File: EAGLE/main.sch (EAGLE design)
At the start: 5 parts

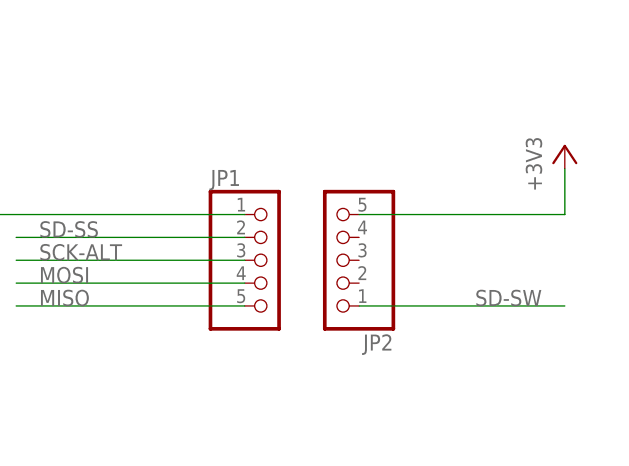
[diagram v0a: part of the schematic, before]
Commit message: Add note about 3V3 solder bridge on SD card PCB
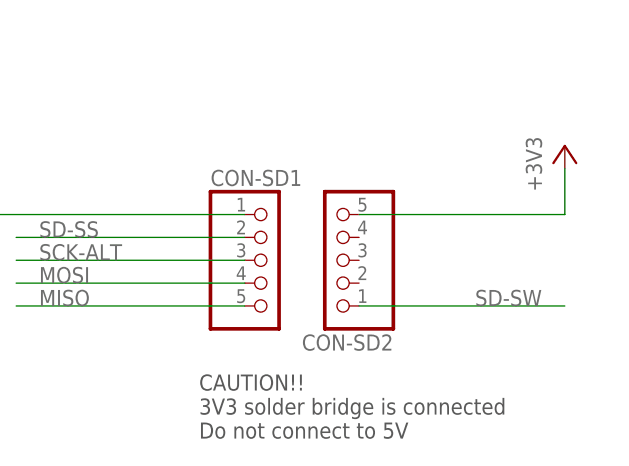
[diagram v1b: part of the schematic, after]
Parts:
- renumbered JP1 to CON-SD1, JP2 to CON-SD2
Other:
- note added: "CAUTION!! 3V3 solder bridge is connected Do not connect to 5V"
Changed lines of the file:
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@@
 <part name="CON-BT" library="pinhead" deviceset="PINHD-1X4" device=""/>
 <part name="CON-GY-80" library="pinhead" deviceset="PINHD-1X4" device=""/>
-<part name="JP1" library="pinhead" deviceset="PINHD-1X5" device=""/>
-<part name="JP2" library="pinhead" deviceset="PINHD-1X5" device=""/>
+<part name="CON-SD1" library="pinhead" deviceset="PINHD-1X5" device=""/>
+<part name="CON-SD2" library="pinhead" deviceset="PINHD-1X5" device=""/>
 <part name="+3V2" library="supply1" deviceset="+3V3" device=""/>
 <part name="GND2" library="supply1" deviceset="GND" device=""/>
@@
 <sheet>
 <plain>
+<text x="149.86" y="55.88" size="1.778" layer="97" rot="MR180">CAUTION!!
+3V3 solder bridge is connected
+Do not connect to 5V</text>
 </plain>
 <instances>
@@
 <instance part="CON-BT" gate="A" x="162.56" y="152.4"/>
 <instance part="CON-GY-80" gate="A" x="162.56" y="111.76"/>
-<instance part="JP1" gate="A" x="157.48" y="68.58"/>
-<instance part="JP2" gate="A" x="165.1" y="68.58" rot="R180"/>
+<instance part="CON-SD1" gate="A" x="157.48" y="68.58"/>
+<instance part="CON-SD2" gate="A" x="165.1" y="68.58" rot="R180"/>
 <instance part="+3V2" gate="G$1" x="132.08" y="121.92"/>
 <instance part="GND2" gate="1" x="132.08" y="109.22"/>
@@
 </segment>
 <segment>
-<pinref part="JP2" gate="A" pin="5"/>
+<pinref part="CON-SD2" gate="A" pin="5"/>
 <wire x1="167.64" y1="73.66" x2="190.5" y2="73.66" width="0.1524" layer="91"/>
 <pinref part="+3V4" gate="G$1" pin="+3V3"/>
@@
 </segment>
 <segment>
-<pinref part="JP1" gate="A" pin="1"/>
+<pinref part="CON-SD1" gate="A" pin="1"/>
 <wire x1="154.94" y1="73.66" x2="124.46" y2="73.66" width="0.1524" layer="91"/>
 <wire x1="124.46" y1="73.66" x2="124.46" y2="71.12" width="0.1524" layer="91"/>
@@
 </segment>
 <segment>
-<pinref part="JP1" gate="A" pin="4"/>
+<pinref part="CON-SD1" gate="A" pin="4"/>
 <wire x1="154.94" y1="66.04" x2="129.54" y2="66.04" width="0.1524" layer="91"/>
 <label x="132.08" y="66.04" size="1.778" layer="95"/>
@@
 </segment>
 <segment>
-<pinref part="JP1" gate="A" pin="5"/>
+<pinref part="CON-SD1" gate="A" pin="5"/>
 <wire x1="154.94" y1="63.5" x2="129.54" y2="63.5" width="0.1524" layer="91"/>
 <label x="132.08" y="63.5" size="1.778" layer="95"/>
@@
 </segment>
 <segment>
-<pinref part="JP1" gate="A" pin="3"/>
+<pinref part="CON-SD1" gate="A" pin="3"/>
 <wire x1="154.94" y1="68.58" x2="129.54" y2="68.58" width="0.1524" layer="91"/>
 <label x="132.08" y="68.58" size="1.778" layer="95"/>
@@
 <net name="SD-SS" class="0">
 <segment>
-<pinref part="JP1" gate="A" pin="2"/>
+<pinref part="CON-SD1" gate="A" pin="2"/>
 <wire x1="154.94" y1="71.12" x2="129.54" y2="71.12" width="0.1524" layer="91"/>
 <label x="132.08" y="71.12" size="1.778" layer="95"/>
@@
 <net name="SD-SW" class="0">
 <segment>
-<pinref part="JP2" gate="A" pin="1"/>
+<pinref part="CON-SD2" gate="A" pin="1"/>
 <wire x1="167.64" y1="63.5" x2="190.5" y2="63.5" width="0.1524" layer="91"/>
 <label x="187.96" y="63.5" size="1.778" layer="95" rot="MR0"/>
@@
 </schematic>
 </drawing>
+<compatibility>
+<note version="6.3" minversion="6.2.2" severity="warning">
+Since Version 6.2.2 text objects can contain more than one line,
+which will not be processed correctly with this version.
+</note>
+</compatibility>
 </eagle>

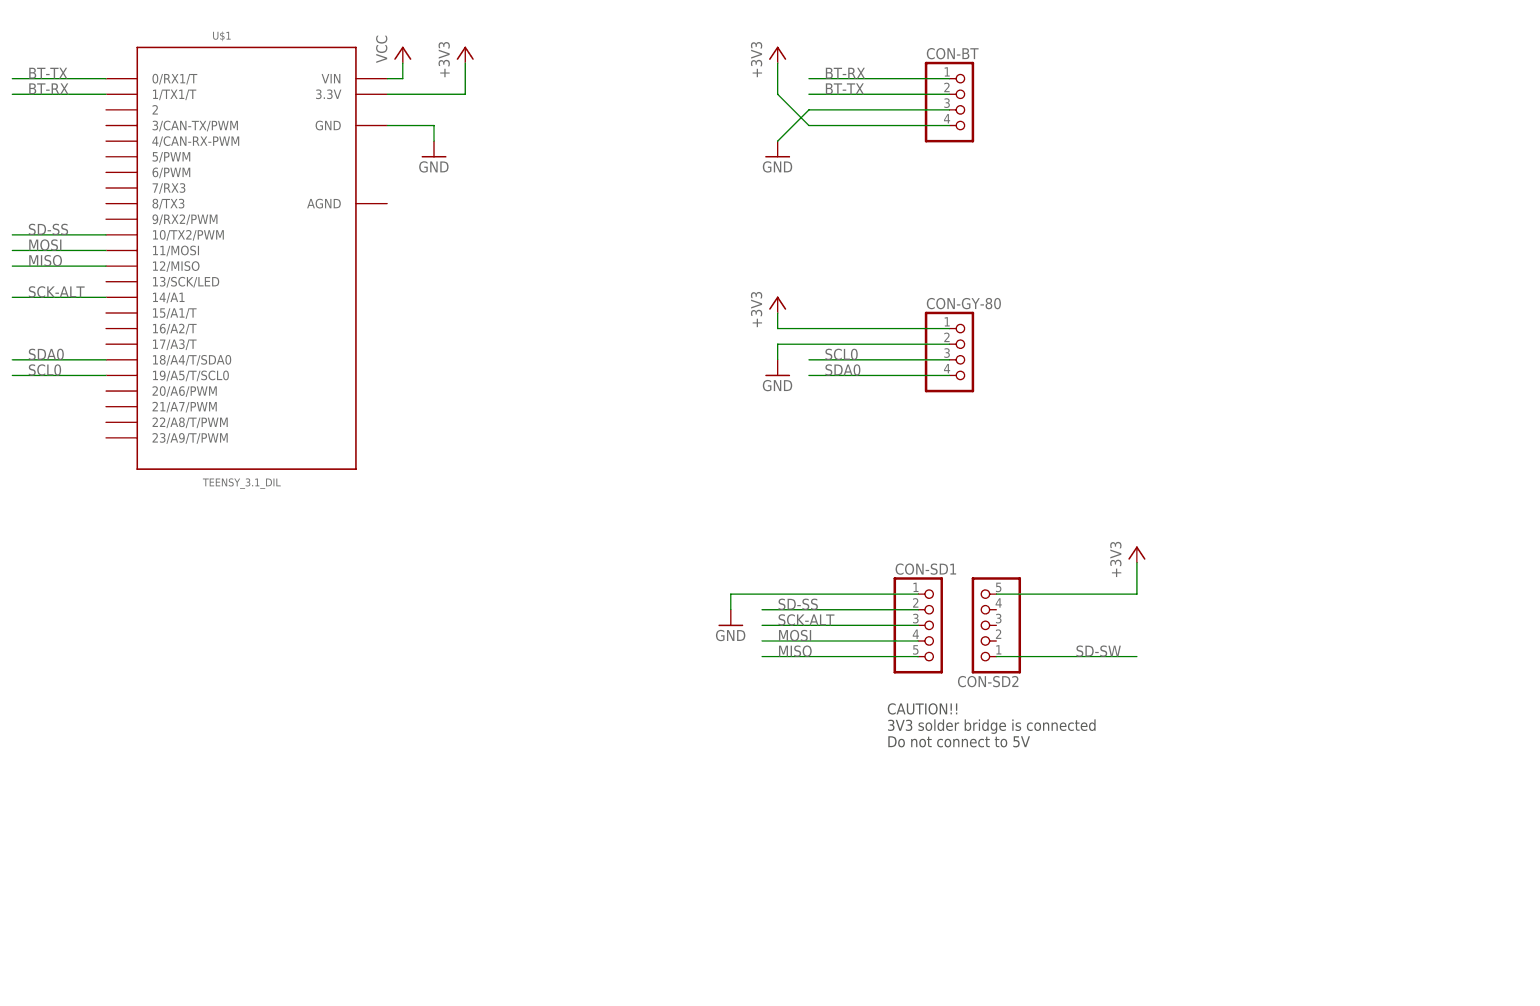
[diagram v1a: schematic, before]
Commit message: Rough sketch of LiPo power supply.
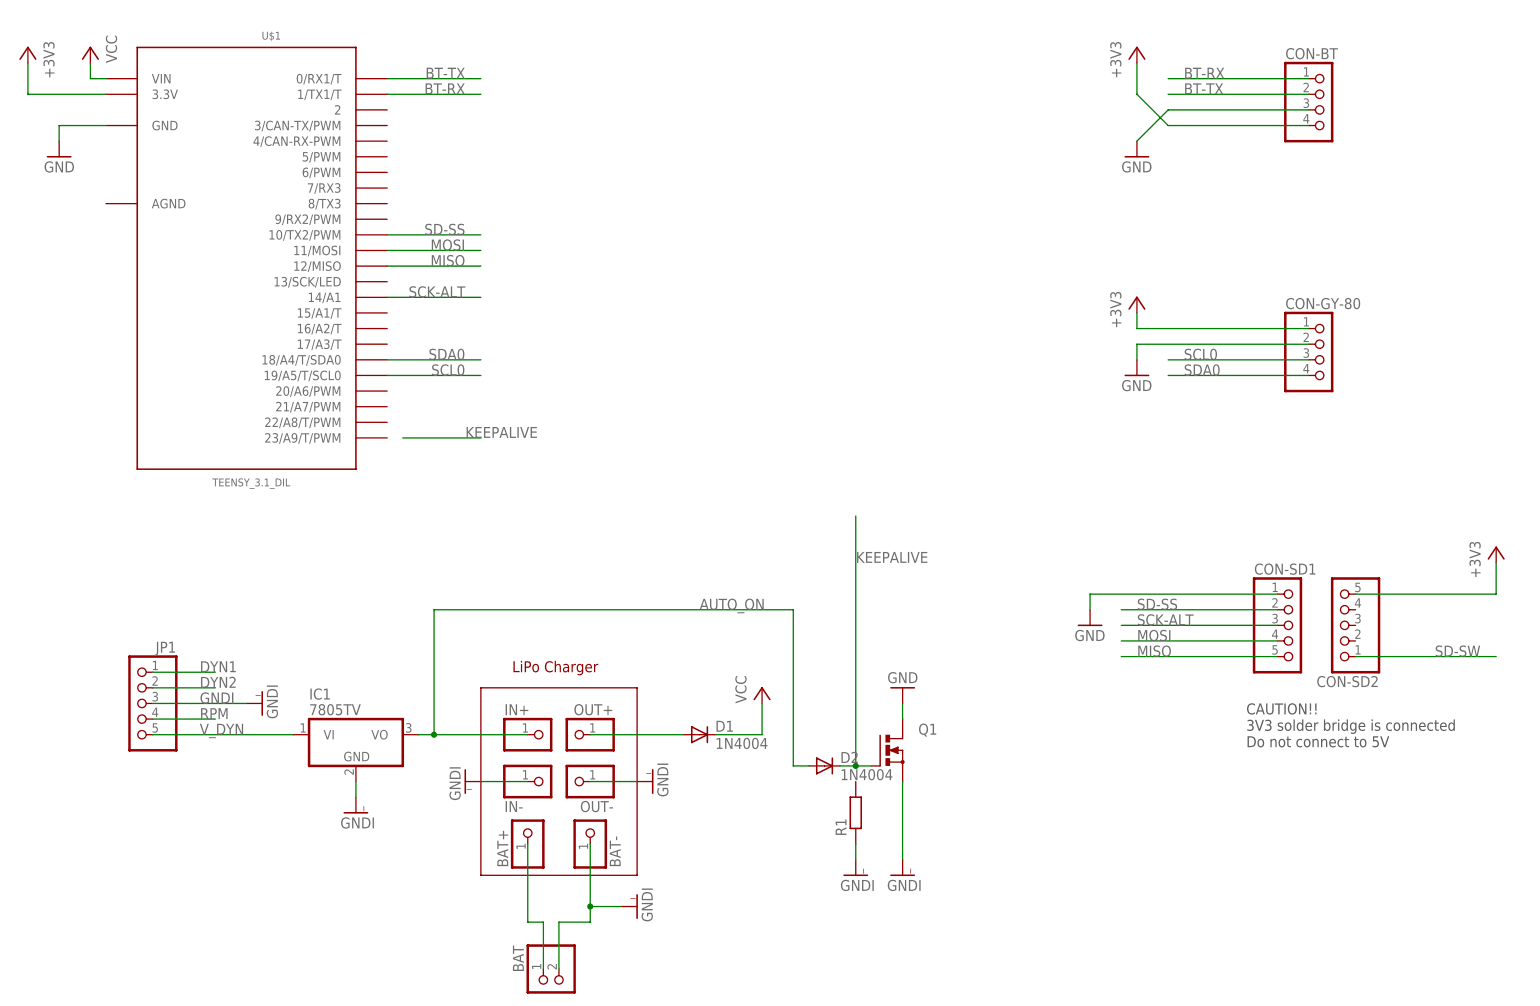
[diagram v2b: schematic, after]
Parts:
- added BAT: (no value), pinhead:PINHD-1X2
- added BAT+, BAT-, IN+, IN-, OUT+, OUT-: (no value), pinhead:PINHD-1X1
- added D1, D2: 1N4004, adafruit:1N4004
- added IC1: 7805TV, linear:7805TV
- added JP1: (no value), pinhead:PINHD-1X5
- added Q1: (no value), transistor-power:PMOSFET_NTO220BV
- added R1: (no value), rcl:R-EU_0204/7
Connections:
- new net AUTO_ON: D2.A, IN+.1
- new net BAT+: BAT+.1, BAT.1
- new net DYN1: JP1.1
- new net DYN2: JP1.2
- new net GNDI: BAT-.1, BAT.2, IC1.GND, IN-.1, JP1.3, OUT-.1, Q1.S, R1.1
- new net KEEPALIVE: D2.C, Q1.G
- new net OUT+: D1.A, OUT+.1
- new net RPM: JP1.4
- new net V_DYN: JP1.5
- net GND: now also Q1.D
- net VCC: now also D1.C
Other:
- note added: "LiPo Charger"
- moved on the sheet: CON-BT, CON-GY-80, CON-SD1, CON-SD2

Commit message: Use MCP1825 as 3.3V regulator
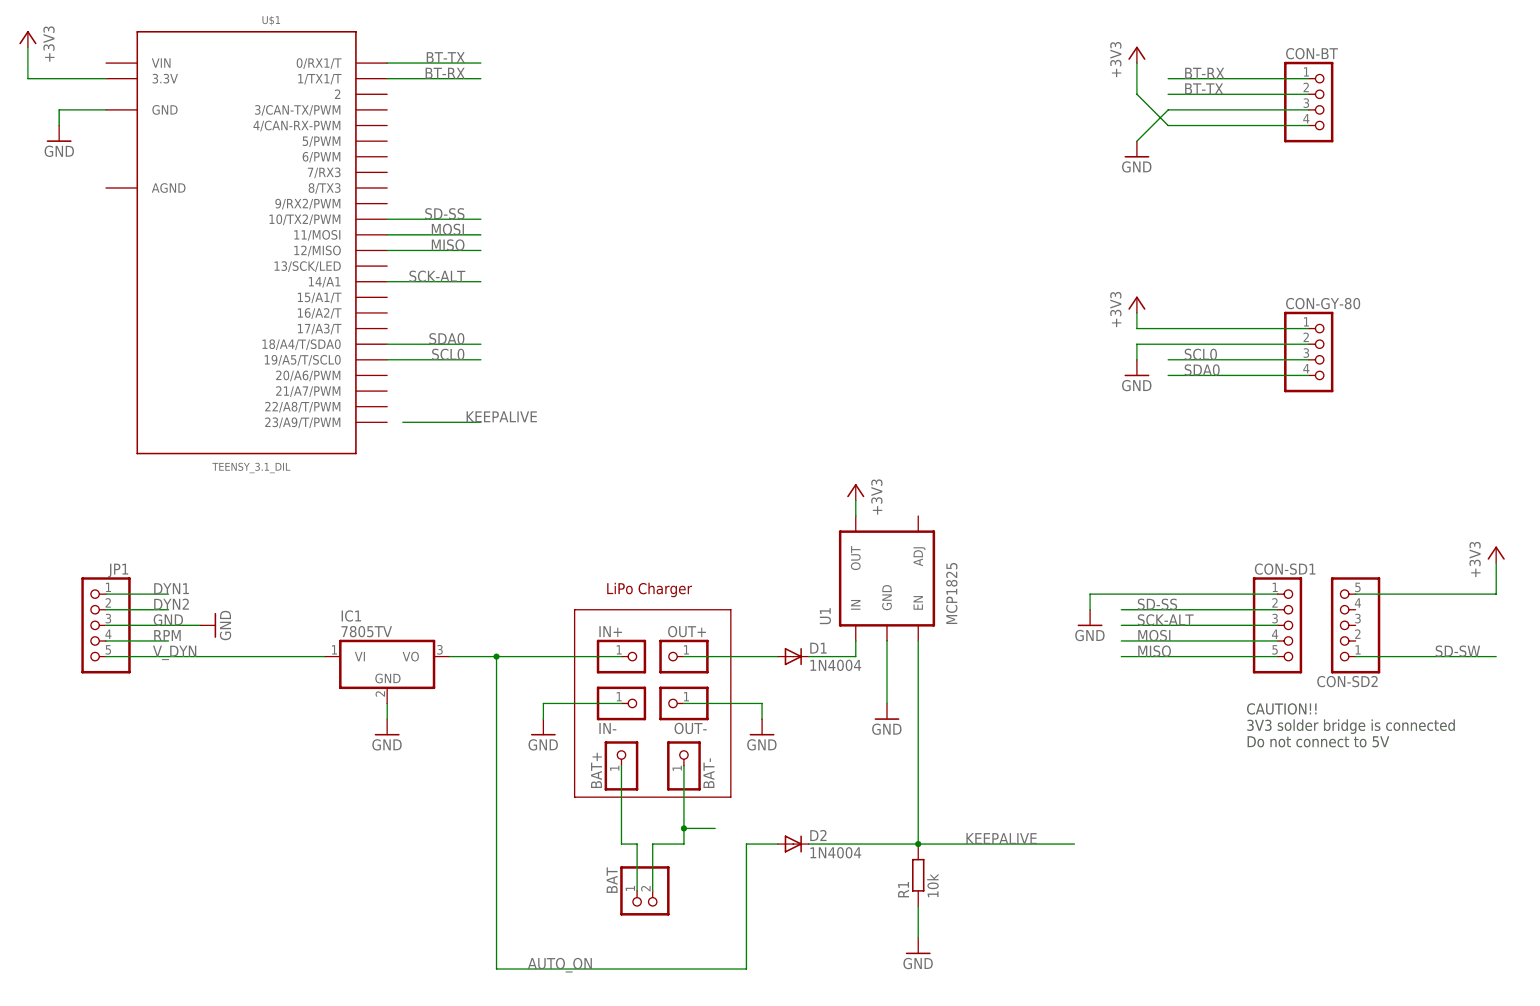
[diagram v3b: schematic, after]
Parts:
- removed Q1: (no value), transistor-power:PMOSFET_NTO220BV
- added U1: MCP1825, bt_regulator:MCP1824
- R1: value (none) -> 10k
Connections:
- removed net GNDI: BAT-.1, BAT.2, IC1.GND, IN-.1, JP1.3, OUT-.1, Q1.S, R1.1
- removed net VCC: D1.C, U$1.VIN
- new net N$2: D1.C, U1.IN
- new net N$5: BAT-.1, BAT.2
- net +3V3: now also U1.OUT
- net AUTO_ON: now also IC1.VO
- net GND: now also IC1.GND, IN-.1, JP1.3, OUT-.1, R1.1, U1.GND; no longer Q1.D
- net KEEPALIVE: now also R1.2, U1.EN; no longer Q1.G
- net V_DYN: now also IC1.VI
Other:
- moved on the sheet: BAT, BAT+, BAT-, D1, D2, IC1, IN+, IN-, JP1, OUT+, OUT-, R1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
